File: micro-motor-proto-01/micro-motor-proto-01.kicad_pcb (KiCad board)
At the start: 2 copper layers, 2 parts, among them J1 PhA, J2 PhB

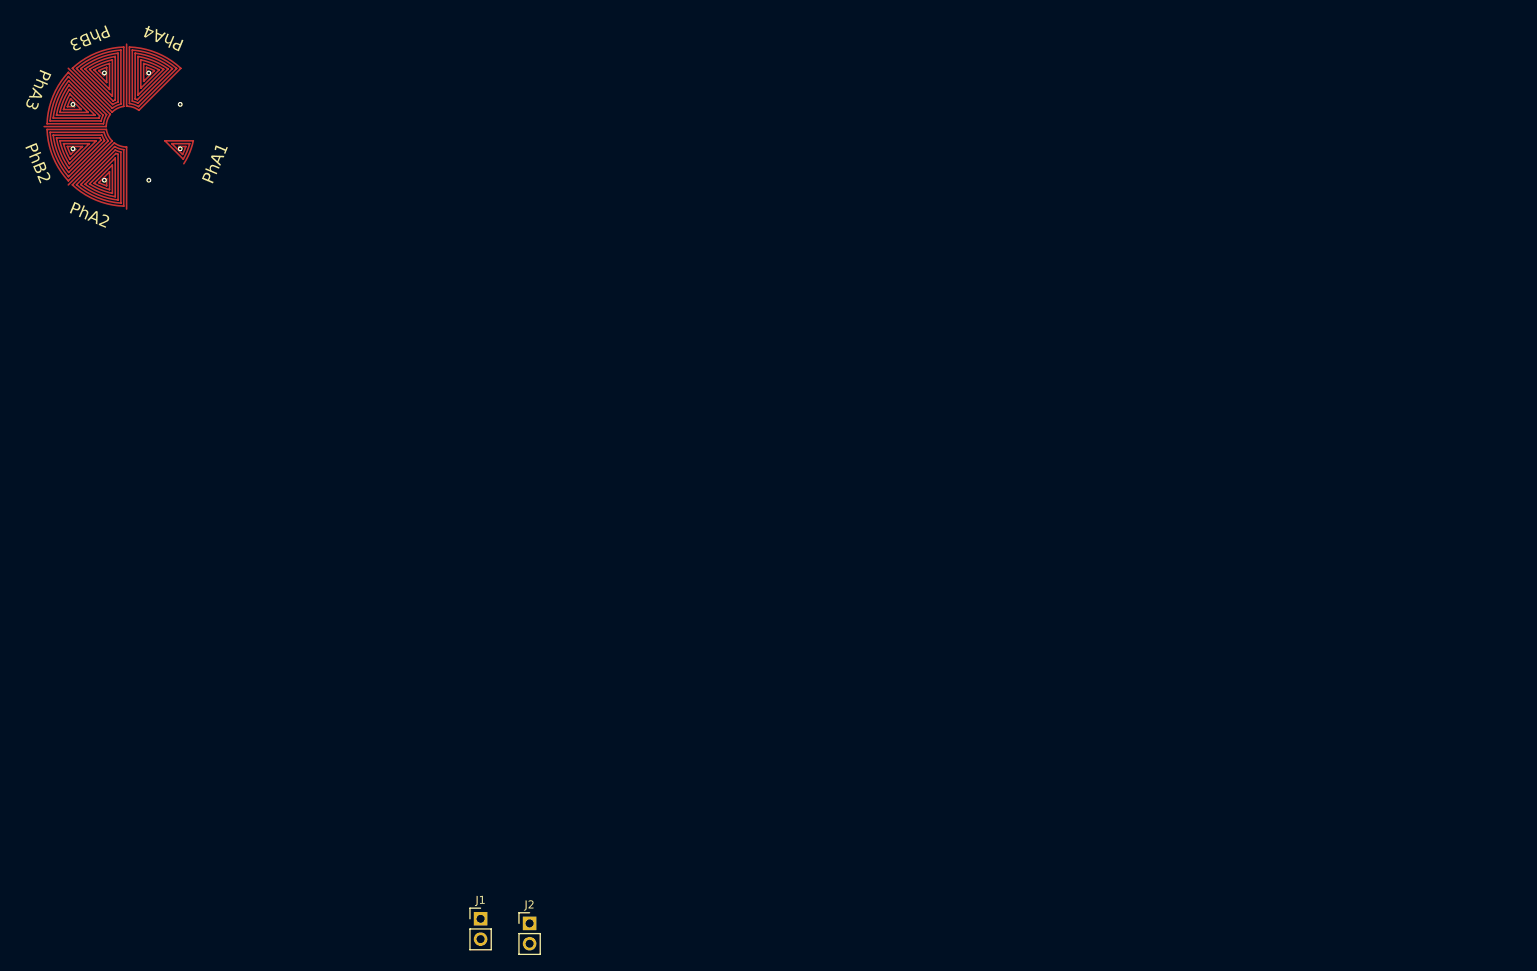
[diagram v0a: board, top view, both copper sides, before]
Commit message: Schematic & layout updates
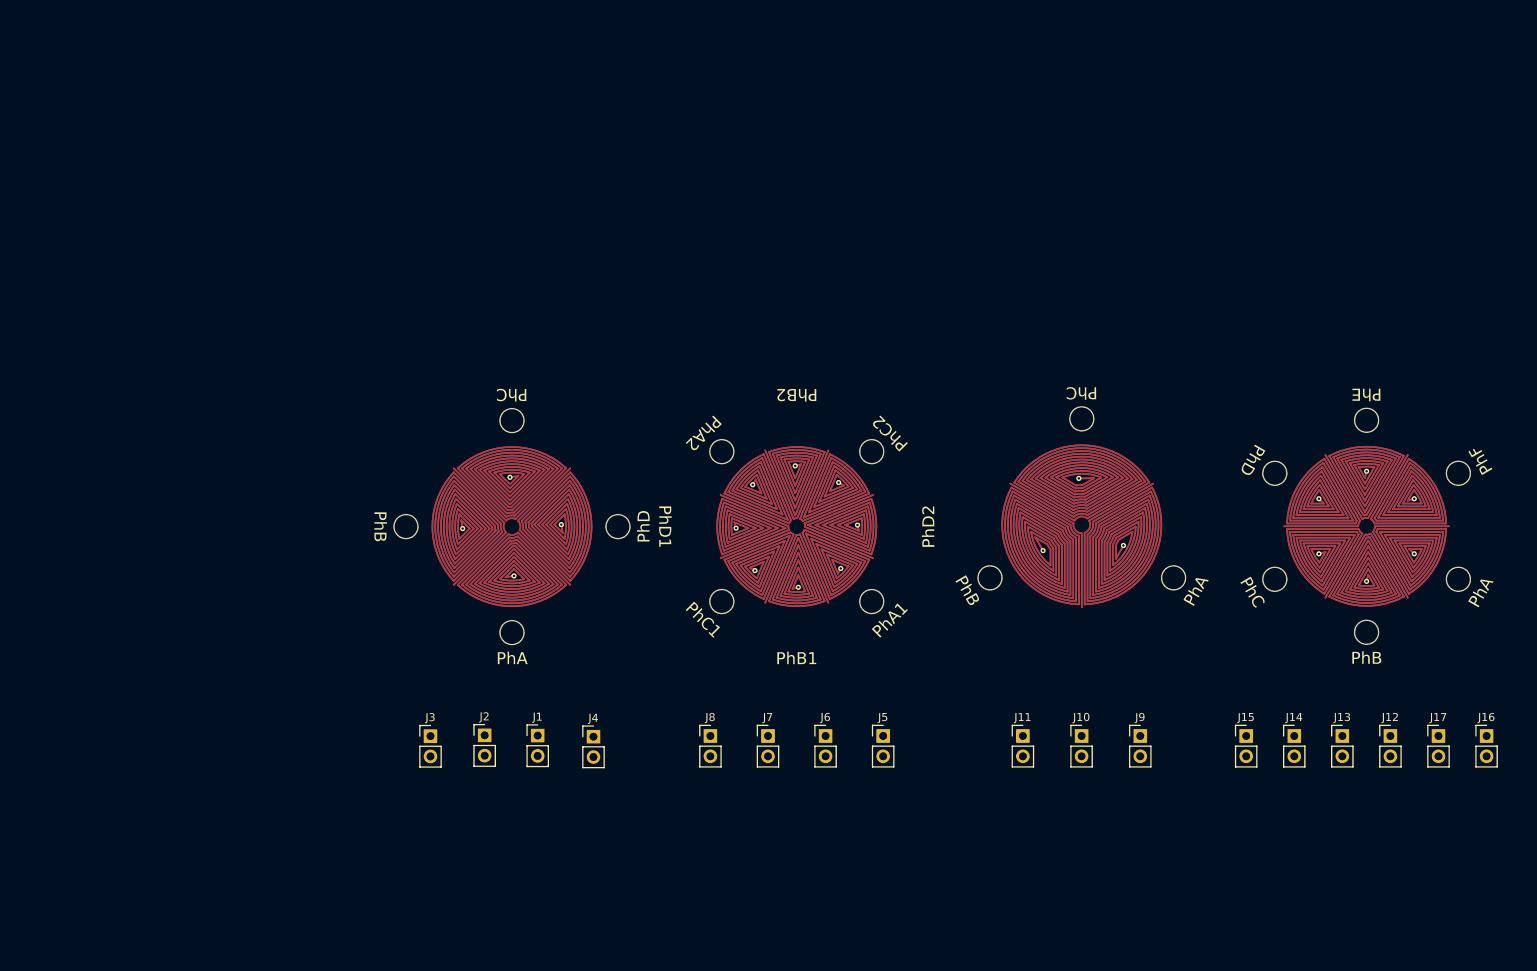
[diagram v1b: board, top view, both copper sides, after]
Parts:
- added J10: PhB, Connector_PinHeader_2.54mm:PinHeader_1x02_P2.54mm_Vertical, F.Cu at (119.4, 76.2)
- added J11: PhC, Connector_PinHeader_2.54mm:PinHeader_1x02_P2.54mm_Vertical, F.Cu at (112.0, 76.2)
- added J12: PhA, Connector_PinHeader_2.54mm:PinHeader_1x02_P2.54mm_Vertical, F.Cu at (158.0, 76.2)
- added J13: PhB, Connector_PinHeader_2.54mm:PinHeader_1x02_P2.54mm_Vertical, F.Cu at (152.0, 76.2)
- added J14: PhC, Connector_PinHeader_2.54mm:PinHeader_1x02_P2.54mm_Vertical, F.Cu at (146.0, 76.2)
- added J15: PhD, Connector_PinHeader_2.54mm:PinHeader_1x02_P2.54mm_Vertical, F.Cu at (139.9, 76.2)
- added J16: PhE, Connector_PinHeader_2.54mm:PinHeader_1x02_P2.54mm_Vertical, F.Cu at (170.0, 76.2)
- added J17: PhF, Connector_PinHeader_2.54mm:PinHeader_1x02_P2.54mm_Vertical, F.Cu at (164.0, 76.2)
- added J3: PhC, Connector_PinHeader_2.54mm:PinHeader_1x02_P2.54mm_Vertical, F.Cu at (38.0, 76.2)
- added J4: PhD, Connector_PinHeader_2.54mm:PinHeader_1x02_P2.54mm_Vertical, F.Cu at (58.4, 76.3)
- added J5: PhA, Connector_PinHeader_2.54mm:PinHeader_1x02_P2.54mm_Vertical, F.Cu at (94.6, 76.2)
- added J6: PhB, Connector_PinHeader_2.54mm:PinHeader_1x02_P2.54mm_Vertical, F.Cu at (87.4, 76.2)
- added J7: PhC, Connector_PinHeader_2.54mm:PinHeader_1x02_P2.54mm_Vertical, F.Cu at (80.2, 76.2)
- added J8: PhD, Connector_PinHeader_2.54mm:PinHeader_1x02_P2.54mm_Vertical, F.Cu at (73.0, 76.2)
- added J9: PhA, Connector_PinHeader_2.54mm:PinHeader_1x02_P2.54mm_Vertical, F.Cu at (126.7, 76.2)
- moved J2 24.2 mm to (44.8, 76.1)
- moved J1 24.0 mm to (51.4, 76.1)
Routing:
- net /3 PhC: track 0.00 -> 581.7 mm, vias 0 -> 1
- net /3 PhB: track 0.00 -> 581.7 mm, vias 0 -> 1
- net /3 PhA: track 0.00 -> 581.7 mm, vias 0 -> 1
- net /2 PhC: track 0.00 -> 443.2 mm, vias 0 -> 1
- net /2 PhD: track 0.00 -> 443.2 mm, vias 0 -> 1
- net /2-8 PhD: track 0.00 -> 442.5 mm, vias 0 -> 2
- net /2-8 PhB: track 0.00 -> 442.5 mm, vias 0 -> 2
- net /2-8 PhC: track 0.00 -> 442.5 mm, vias 0 -> 2
- net /2-8 PhA: track 0.00 -> 442.5 mm, vias 0 -> 2
- net /3-6 PhD: track 0.00 -> 296.1 mm, vias 0 -> 1
- net /3-6 PhA: track 0.00 -> 296.1 mm, vias 0 -> 1
- net /3-6 PhF: track 0.00 -> 296.1 mm, vias 0 -> 1
- net /3-6 PhC: track 0.00 -> 296.1 mm, vias 0 -> 1
- net /3-6 PhB: track 0.00 -> 296.1 mm, vias 0 -> 1
- net /3-6 PhE: track 0.00 -> 296.1 mm, vias 0 -> 1
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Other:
- board outline added: 134.6 x 29.7 mm
- board text added: "PhA"
- board text added: "PhB"
- board text added: "PhB1"
- board text added: "PhC"
- board text added: "PhC1"
- board text added: "PhC2"
- board text added: "PhD"
- board text added: "PhD1"
- board text added: "PhD2"
- board text added: "PhE"
- board text added: "PhF"
- board text removed: "PhA3"
- board text removed: "PhA4"
- board text removed: "PhB3"

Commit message: Routing complete.
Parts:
- moved J16 29.7 mm to (140.3, 76.2)
- moved J15 6.21 mm to (146.2, 76.2)
- moved J14 6.08 mm to (152.0, 76.2)
- moved J13 5.94 mm to (157.9, 76.2)
- moved J12 5.81 mm to (163.8, 76.2)
- moved J17 5.67 mm to (169.7, 76.2)
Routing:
- net /2-8 PhD: track 442.5 -> 592.6 mm, vias 2 -> 5
- net /2-8 PhA: track 442.5 -> 569.1 mm
- net /2-8 PhC: track 442.5 -> 564.0 mm, vias 2 -> 7
- net /2-8 PhB: track 442.5 -> 563.9 mm, vias 2 -> 6
- net /3-6 PhE: track 296.1 -> 393.1 mm
- net /3-6 PhF: track 296.1 -> 392.1 mm
- net /3 PhA: track 581.7 -> 663.9 mm
- net /3 PhC: track 581.7 -> 663.7 mm
- net /2 PhD: track 443.2 -> 519.9 mm
- net /2 PhC: track 443.2 -> 519.8 mm
- net /3-6 PhD: track 296.1 -> 362.7 mm
- net /3-6 PhA: track 296.1 -> 362.1 mm
- net /2 PhB: track 443.2 -> 490.2 mm
- net /2 PhA: track 443.2 -> 489.8 mm
- net /3-6 PhC: track 296.1 -> 338.5 mm
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
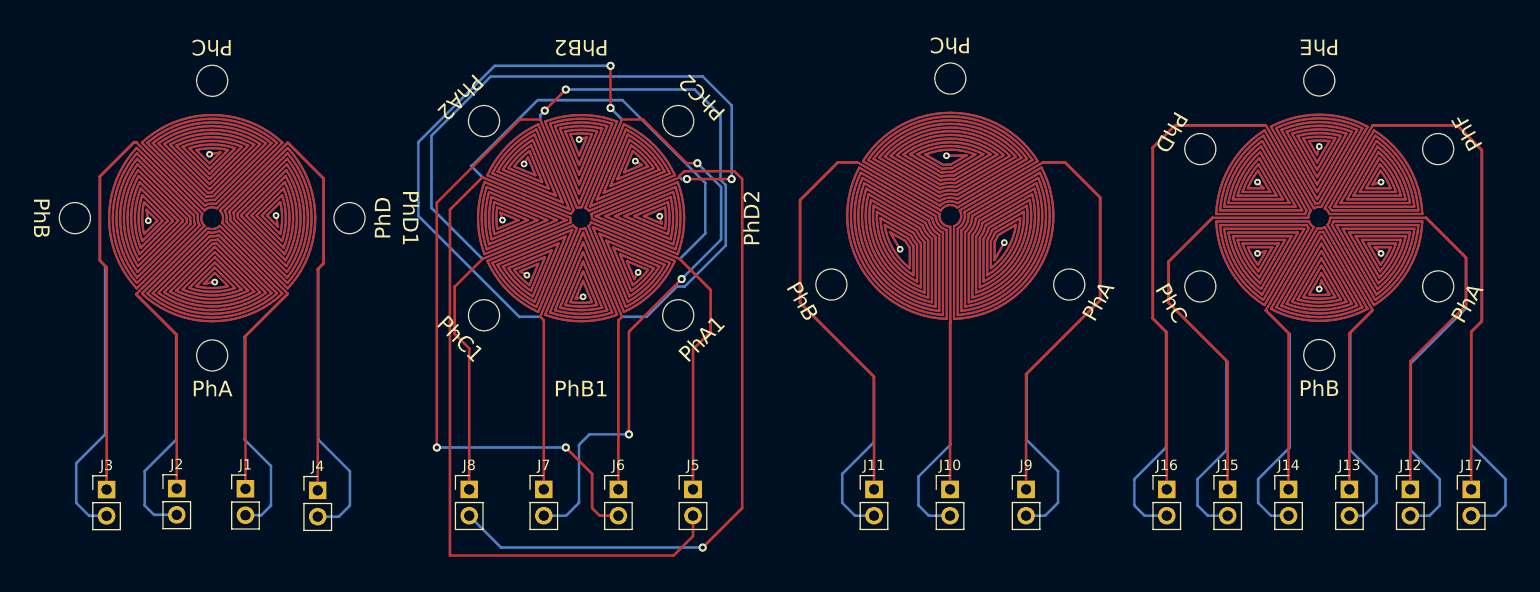
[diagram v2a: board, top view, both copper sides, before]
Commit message: Rev 2 board, swapped bottom layer coil direction.
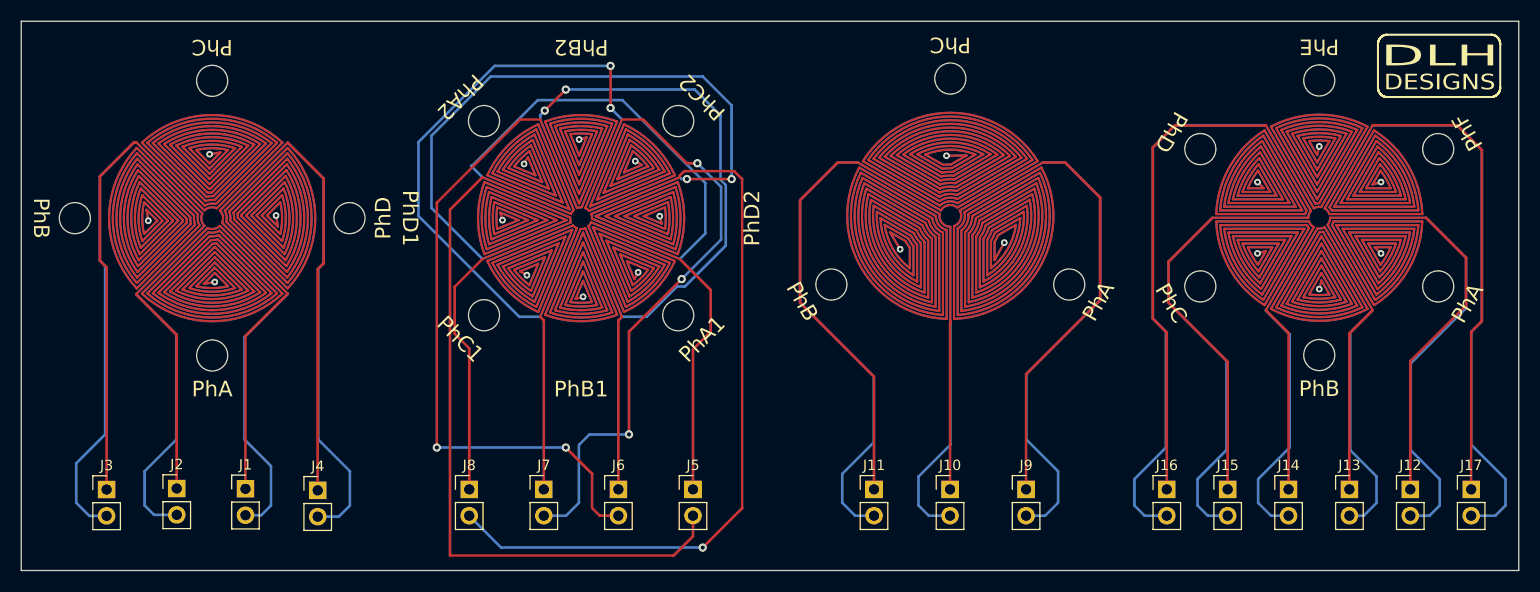
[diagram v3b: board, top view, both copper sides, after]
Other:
- board size 134.6 x 29.7 mm -> 144.5 x 53 mm
- board text added: "DESIGNS"
- board text added: "DLH"
